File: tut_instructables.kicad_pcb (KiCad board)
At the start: 2 copper layers, 42.5 x 36 mm, 30 parts, among them J1 USB4110GFA, SW1 CK_KMS2xxGP, SW2 CK_KMS2xxGP, U1 AMS1117-3.3, U2 ESP32-C3-WROOM-02

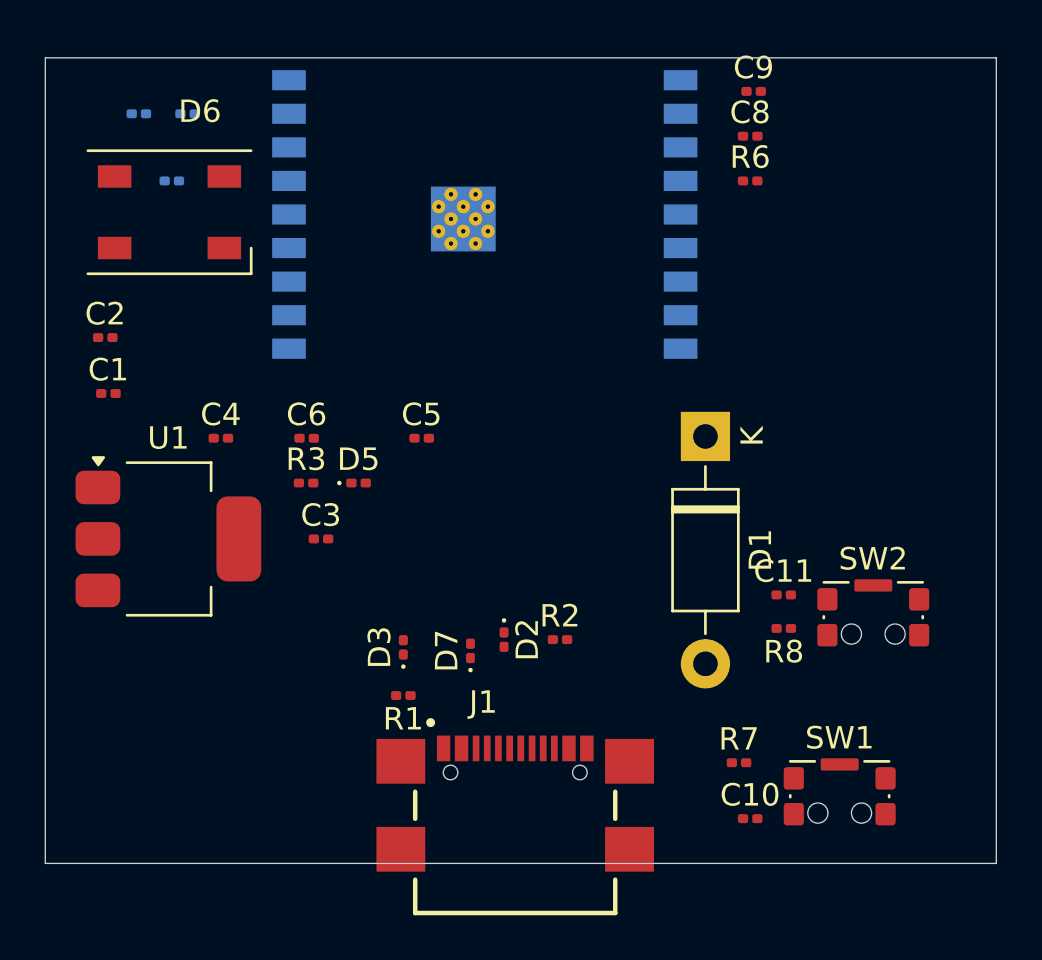
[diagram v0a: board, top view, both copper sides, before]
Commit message: added all the footprints
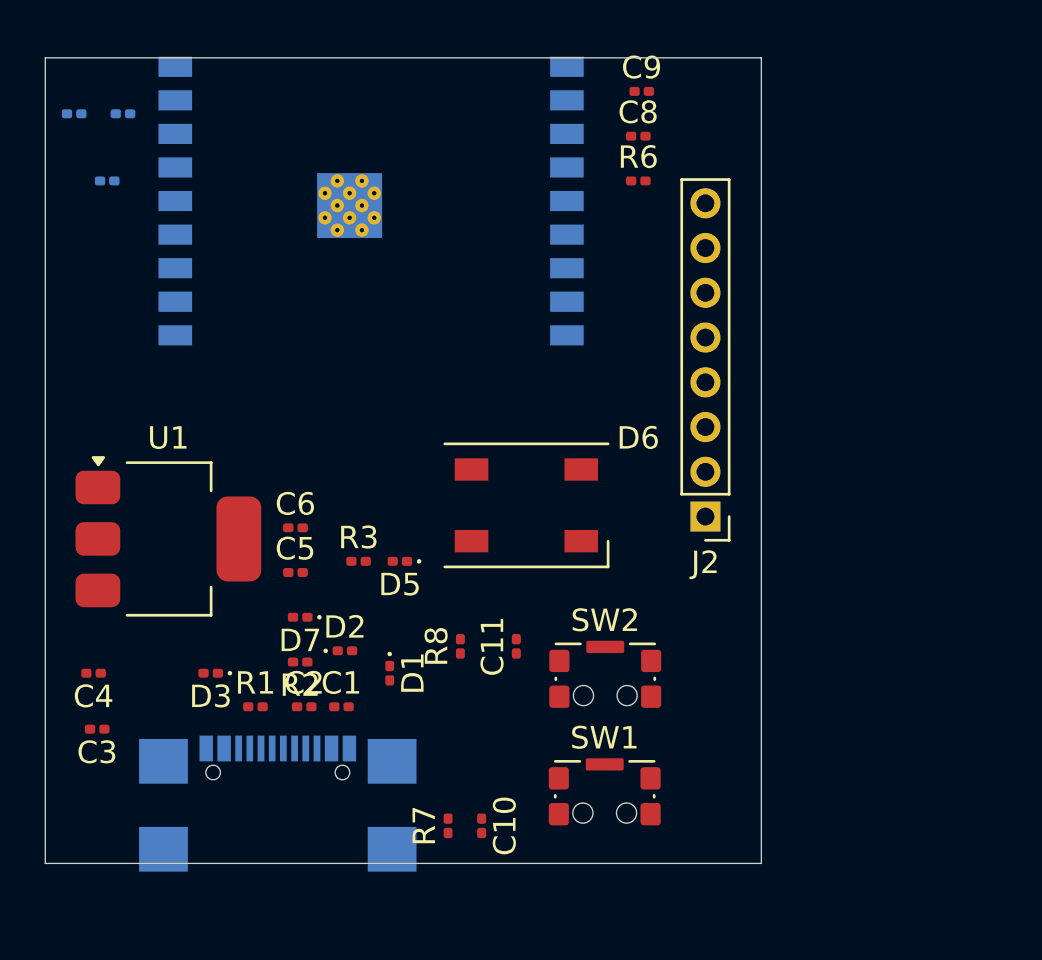
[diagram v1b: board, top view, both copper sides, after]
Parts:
- added J2: Conn_01x08_Pin, Connector_PinHeader_2.00mm:PinHeader_1x08_P2.00mm_Vertical, F.Cu at (76.5, 65.5)
- D1: footprint Diode_THT:D_DO-41_SOD81_P10.16mm_Horizontal -> Diode_SMD:D_0201_0603Metric
- J1: moved to B.Cu
- R2: value R -> 5K
- moved D6 20.6 mm to (68.5, 65.0)
- moved C2 18.7 mm to (58.6, 74.0)
- moved D1 17.6 mm to (62.4, 72.5)
- moved C1 17.4 mm to (60.2, 74.0)
- moved R8 14.5 mm to (65.5, 71.3), turned to 90 degrees
- moved R7 13.3 mm to (65.0, 79.3), turned to 90 degrees
- moved C3 13.1 mm to (49.3, 75.0), turned to 180 degrees
- moved SW2 12.3 mm to (72.0, 72.8)
- moved C11 12.2 mm to (68.0, 71.3), turned to 90 degrees
- moved C10 12.0 mm to (66.5, 79.3), turned to -90 degrees
- moved C4 11.9 mm to (49.2, 72.5), turned to 180 degrees
- moved R2 11.7 mm to (58.4, 72.0), turned to 180 degrees
- moved J1 10.6 mm to (57.4, 76.9), turned to 180 degrees
- moved SW1 10.5 mm to (72.0, 78.0)
- moved D3 8.69 mm to (54.4, 72.5), turned to 180 degrees
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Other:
- board size 42.5 x 36 mm -> 32 x 36 mm

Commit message: stated routing the pcb
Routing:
- net VCC_5V: track 0.00 -> 22.5 mm
- net /D-: track 0.00 -> 9.33 mm
- net ESP_3v3: track 0.00 -> 8.49 mm
- net /D+: track 0.00 -> 6.50 mm
- net Net-(J1-CC1): track 0.00 -> 3.96 mm
- net Net-(D1-A): track 0.00 -> 3.62 mm
- net Net-(D5-A): track 0.00 -> 1.20 mm
